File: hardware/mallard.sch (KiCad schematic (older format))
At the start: 0 parts

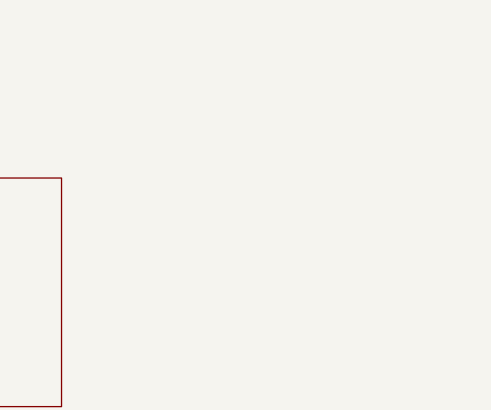
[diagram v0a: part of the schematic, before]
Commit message: Added resistors
Added resistors to top level elements
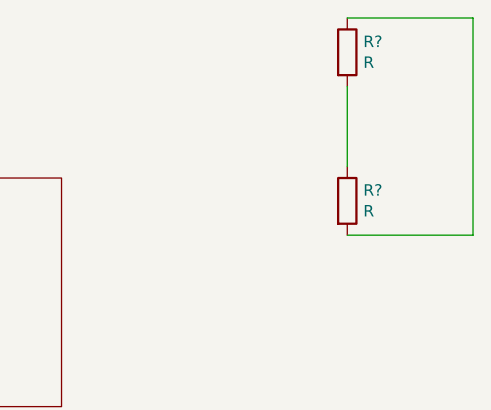
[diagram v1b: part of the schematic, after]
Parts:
- added R? (x2): R, symbol Device:R
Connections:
- new net: R?.1, R?.2 (x2)
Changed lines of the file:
@@
 $Descr A4 11693 8268
 encoding utf-8
-Sheet 1 3
+Sheet 1 4
 Title ""
 Date ""
@@
 F1 "power.sch" 50
 $EndSheet
+$Comp
+L Device:R R?
+U 1 1 60DFA6CD
+P 8750 1950
+F 0 "R?" H 8820 1996 50  0000 L CNN
+F 1 "R" H 8820 1905 50  0000 L CNN
+F 2 "" V 8680 1950 50  0001 C CNN
+F 3 "~" H 8750 1950 50  0001 C CNN
+	1    8750 1950
+	1    0    0    -1
+$EndComp
+$Comp
+L Device:R R?
+U 1 1 60DFB454
+P 8750 2600
+F 0 "R?" H 8820 2646 50  0000 L CNN
+F 1 "R" H 8820 2555 50  0000 L CNN
+F 2 "" V 8680 2600 50  0001 C CNN
+F 3 "~" H 8750 2600 50  0001 C CNN
+	1    8750 2600
+	1    0    0    -1
+$EndComp
+Wire Wire Line
+	8750 2450 8750 2100
+Wire Wire Line
+	8750 1800 9300 1800
+Wire Wire Line
+	9300 2750 8750 2750
+Wire Wire Line
+	9300 1800 9300 2750
 $EndSCHEMATC

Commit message: Removed Resistors
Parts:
- removed R? (x2): R, symbol Device:R
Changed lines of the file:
@@
 F1 "power.sch" 50
 $EndSheet
-$Comp
-L Device:R R?
-U 1 1 60DFA6CD
-P 8750 1950
-F 0 "R?" H 8820 1996 50  0000 L CNN
-F 1 "R" H 8820 1905 50  0000 L CNN
-F 2 "" V 8680 1950 50  0001 C CNN
-F 3 "~" H 8750 1950 50  0001 C CNN
-	1    8750 1950
-	1    0    0    -1
-$EndComp
-$Comp
-L Device:R R?
-U 1 1 60DFB454
-P 8750 2600
-F 0 "R?" H 8820 2646 50  0000 L CNN
-F 1 "R" H 8820 2555 50  0000 L CNN
-F 2 "" V 8680 2600 50  0001 C CNN
-F 3 "~" H 8750 2600 50  0001 C CNN
-	1    8750 2600
-	1    0    0    -1
-$EndComp
-Wire Wire Line
-	8750 2450 8750 2100
-Wire Wire Line
-	8750 1800 9300 1800
-Wire Wire Line
-	9300 2750 8750 2750
-Wire Wire Line
-	9300 1800 9300 2750
 $EndSCHEMATC
